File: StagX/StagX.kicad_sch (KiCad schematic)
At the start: 0 parts

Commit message: feat(TopLevel): added sheets to toplevel diagram
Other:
- added sheet Accumulator (Accumulator.kicad_sch)
- added sheet Dash Box (DashBox.kicad_sch)
- added sheet Inverter & Motor (InverterMotor.kicad_sch)
- added sheet LV Shelf (LVShelf.kicad_sch)
- added sheet PDM (PDM.kicad_sch)
- added sheet Pedal Box (PedalBox.kicad_sch)
- note added: "FIREWALL"
- note added: "LV Battery"
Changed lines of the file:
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@@
     (comment 4 "N/A")
+  )
+  (rectangle (start 130.175 12.7) (end 130.175 198.755)
+    (stroke (width 1) (type dot) (color 255 0 0 1))
+    (fill (type none))
+  )
+  (rectangle (start 20.955 24.13) (end 60.325 48.26)
+    (stroke (width 0) (type default) (color 0 255 255 1))
+    (fill (type none))
+  )
+  (text "LV Battery" (at 36.195 23.495 0)
+    (effects (font (size 1.27 1.27) bold (color 0 0 0 1)) (justify left bottom))
+  )
+  (text "FIREWALL" (at 131.445 14.605 0)
+    (effects (font (size 1.27 1.27) (thickness 0.254) bold (color 255 0 0 1)) (justify left bottom))
+  )
+  (sheet (at 18.415 99.06) (size 27.305 20.32) (fields_autoplaced)
+    (stroke (width 0.1524) (type solid))
+    (fill (color 0 0 0 0.0000))
+    (property "Sheetname" "Inverter & Motor" (at 18.415 98.3484 0)
+      (effects (font (size 1.27 1.27)) (justify left bottom))
+    )
+    (property "Sheetfile" "InverterMotor.kicad_sch" (at 18.415 119.9646 0)
+      (effects (font (size 1.27 1.27)) (justify left top))
+    )
+    (instances
+      (project "StagX"
+        (path "/f802a14a-9970-4775-97a5-629bebb8e9f9" (page "4"))
+      )
+    )
+  )
+  (sheet (at 18.415 72.39) (size 27.305 21.59) (fields_autoplaced)
+    (stroke (width 0.1524) (type solid))
+    (fill (color 0 0 0 0.0000))
+    (property "Sheetname" "LV Shelf" (at 18.415 71.6784 0)
+      (effects (font (size 1.27 1.27)) (justify left bottom))
+    )
+    (property "Sheetfile" "LVShelf.kicad_sch" (at 18.415 94.5646 0)
+      (effects (font (size 1.27 1.27)) (justify left top))
+    )
+    (instances
+      (project "StagX"
+        (path "/f802a14a-9970-4775-97a5-629bebb8e9f9" (page "3"))
+      )
+    )
+  )
+  (sheet (at 90.805 72.39) (size 34.925 46.99) (fields_autoplaced)
+    (stroke (width 0.1524) (type solid))
+    (fill (color 0 0 0 0.0000))
+    (property "Sheetname" "Accumulator" (at 90.805 71.6784 0)
+      (effects (font (size 1.27 1.27)) (justify left bottom))
+    )
+    (property "Sheetfile" "Accumulator.kicad_sch" (at 90.805 119.9646 0)
+      (effects (font (size 1.27 1.27)) (justify left top))
+    )
+    (instances
+      (project "StagX"
+        (path "/f802a14a-9970-4775-97a5-629bebb8e9f9" (page "2"))
+      )
+    )
+  )
+  (sheet (at 74.295 26.67) (size 34.29 17.78) (fields_autoplaced)
+    (stroke (width 0.1524) (type solid))
+    (fill (color 0 0 0 0.0000))
+    (property "Sheetname" "PDM" (at 74.295 25.9584 0)
+      (effects (font (size 1.27 1.27)) (justify left bottom))
+    )
+    (property "Sheetfile" "PDM.kicad_sch" (at 74.295 45.0346 0)
+      (effects (font (size 1.27 1.27)) (justify left top))
+    )
+    (instances
+      (project "StagX"
+        (path "/f802a14a-9970-4775-97a5-629bebb8e9f9" (page "5"))
+      )
+    )
+  )
+  (sheet (at 252.73 72.39) (size 18.415 32.385) (fields_autoplaced)
+    (stroke (width 0.1524) (type solid))
+    (fill (color 0 0 0 0.0000))
+    (property "Sheetname" "Pedal Box" (at 252.73 71.6784 0)
+      (effects (font (size 1.27 1.27)) (justify left bottom))
+    )
+    (property "Sheetfile" "PedalBox.kicad_sch" (at 252.73 105.3596 0)
+      (effects (font (size 1.27 1.27)) (justify left top))
+    )
+    (instances
+      (project "StagX"
+        (path "/f802a14a-9970-4775-97a5-629bebb8e9f9" (page "7"))
+      )
+    )
+  )
+  (sheet (at 197.485 73.025) (size 20.32 44.45) (fields_autoplaced)
+    (stroke (width 0.1524) (type solid))
+    (fill (color 0 0 0 0.0000))
+    (property "Sheetname" "Dash Box" (at 197.485 72.3134 0)
+      (effects (font (size 1.27 1.27)) (justify left bottom))
+    )
+    (property "Sheetfile" "DashBox.kicad_sch" (at 197.485 118.0596 0)
+      (effects (font (size 1.27 1.27)) (justify left top))
+    )
+    (instances
+      (project "StagX"
+        (path "/f802a14a-9970-4775-97a5-629bebb8e9f9" (page "6"))
+      )
+    )
   )
   (sheet_instances

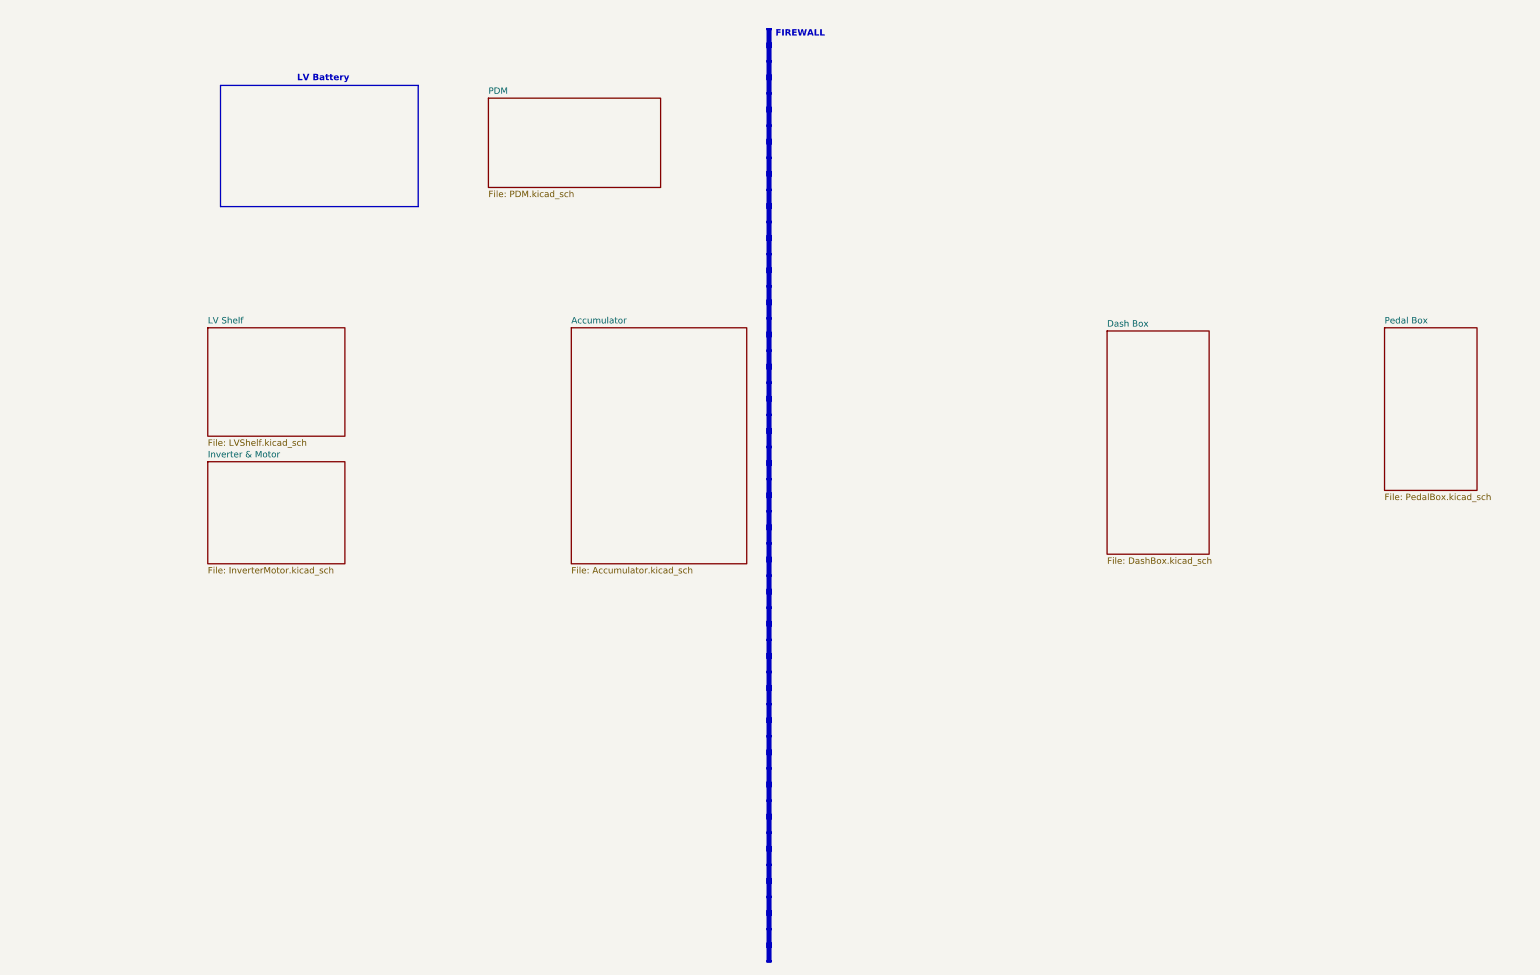
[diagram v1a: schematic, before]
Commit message: feat(RearLoom): Completed Side Pannel Wiring
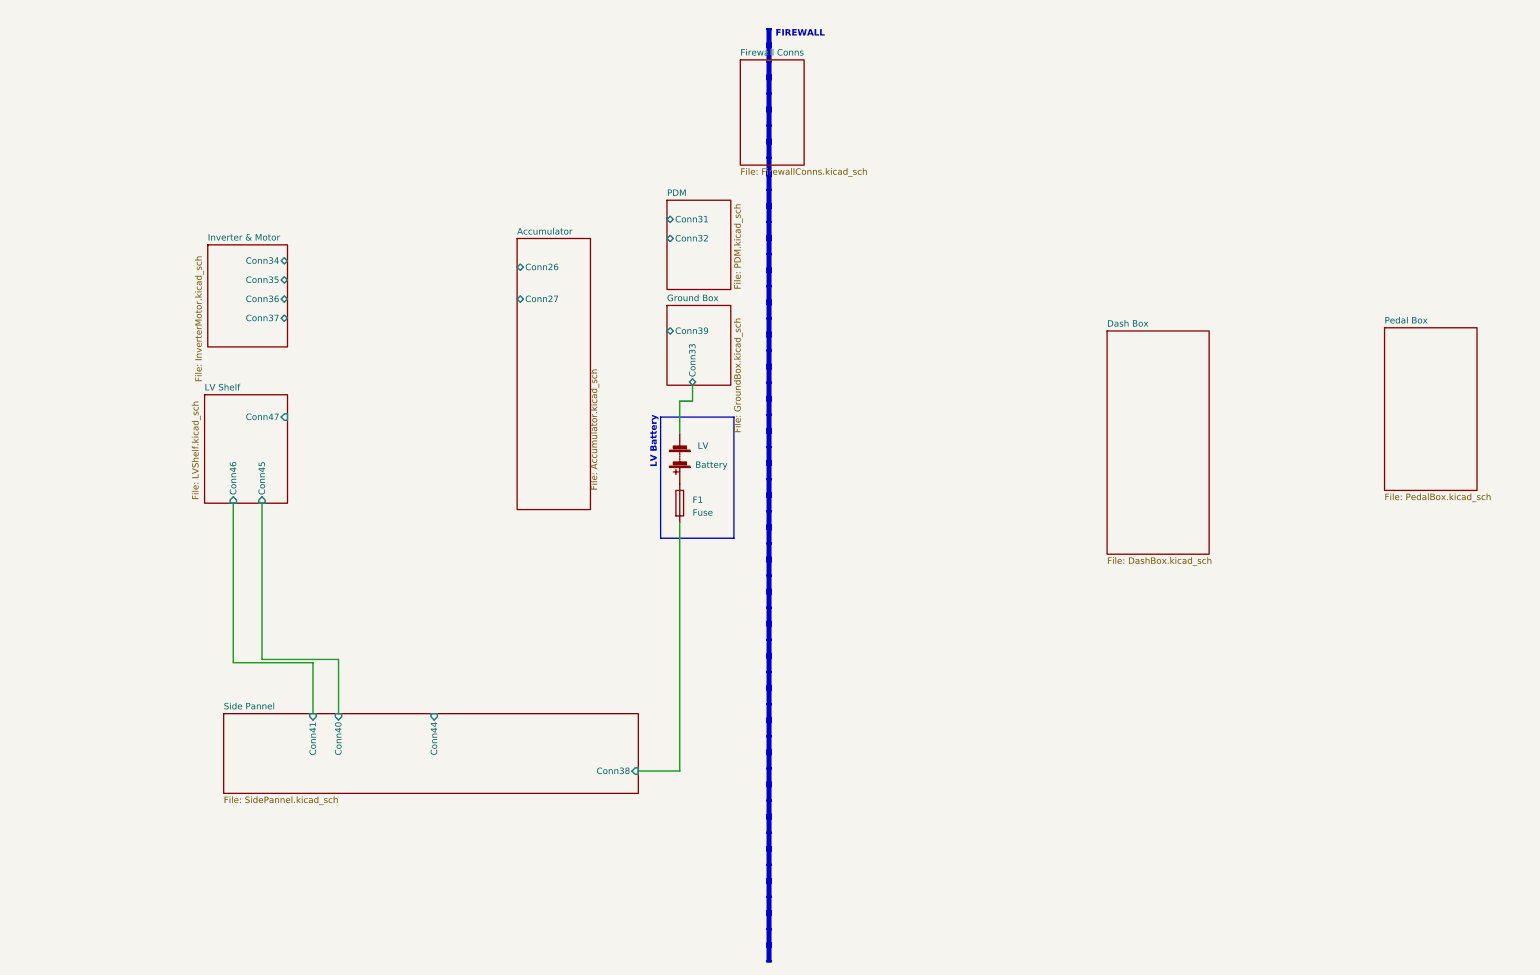
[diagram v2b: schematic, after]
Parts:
- added F1: Fuse, symbol Device:Fuse
- added LV: Battery, symbol Device:Battery
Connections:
- new net: F1.1, LV.1 (+)
- new net Ground Box/Conn33: LV.2 (-)
- new net Side Pannel/Conn38: F1.2
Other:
- added sheet Firewall Conns (FirewallConns.kicad_sch)
- added sheet Ground Box (GroundBox.kicad_sch)
- added sheet Side Pannel (SidePannel.kicad_sch)
- sheet Accumulator ports: added Conn26, Conn27; removed none
- sheet Inverter & Motor ports: added Conn34, Conn35, Conn36, Conn37; removed none
- sheet LV Shelf ports: added Conn45, Conn46, Conn47; removed none
- sheet PDM ports: added Conn31, Conn32; removed none

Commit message: feat(RearLoom): made progress with rear elec box. TSAL LED conns missing
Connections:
- net Ground Box/Conn33 renamed Ground Box/Conn64
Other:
- sheet Ground Box ports: added Conn64, Conn65; removed Conn33, Conn39
- sheet PDM ports: added Conn33; removed none
- sheet Side Pannel ports: added Conn39; removed none
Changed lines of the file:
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@@
+    (stroke (width 0) (type default))
+  )
+  (wire (pts (xy 104.14 154.94) (xy 105.41 154.94))
+    (stroke (width 0) (type default))
+  )
+  (wire (pts (xy 105.41 59.69) (xy 109.855 59.69))
+    (stroke (width 0) (type default))
+  )
+  (wire (pts (xy 105.41 154.94) (xy 105.41 59.69))
     (stroke (width 0) (type default))
   )
@@
       (effects (font (size 1.27 1.27)) (justify right))
     )
+    (pin "Conn39" input (at 104.14 154.94 0)
+      (effects (font (size 1.27 1.27)) (justify right))
+    )
     (instances
       (project "StagX"
@@
       (effects (font (size 1.27 1.27)) (justify left top))
     )
-    (pin "Conn33" bidirectional (at 114.935 83.82 270)
-      (effects (font (size 1.27 1.27)) (justify left))
-    )
-    (pin "Conn39" bidirectional (at 109.855 73.025 180)
+    (pin "Conn64" bidirectional (at 114.935 83.82 270)
+      (effects (font (size 1.27 1.27)) (justify left))
+    )
+    (pin "Conn65" bidirectional (at 109.855 71.755 180)
       (effects (font (size 1.27 1.27)) (justify left))
     )
@@
       (effects (font (size 1.27 1.27)) (justify left))
     )
-    (pin "Conn32" bidirectional (at 109.855 54.61 180)
-      (effects (font (size 1.27 1.27)) (justify left))
-    )
+    (pin "Conn32" bidirectional (at 109.855 55.245 180)
+      (effects (font (size 1.27 1.27)) (justify left))
+    )
+    (pin "Conn33" bidirectional (at 109.855 59.69 180)
+      (effects (font (size 1.27 1.27)) (justify left))
+    )
